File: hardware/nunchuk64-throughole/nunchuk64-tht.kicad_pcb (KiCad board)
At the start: 2 copper layers, 50 x 41.6 mm, 21 parts, among them J1 DB9_Female, J2 DB9_Female, J3 Conn_02x03_Odd_Even, P1 CONN_WII, P2 CONN_WII, Q1 2N7000, Q2 2N7000, Q3 2N7000, Q4 2N7000, SW1 SW_Push, U1 LP2950-3.3_TO92, U2 ATmega328P-PU

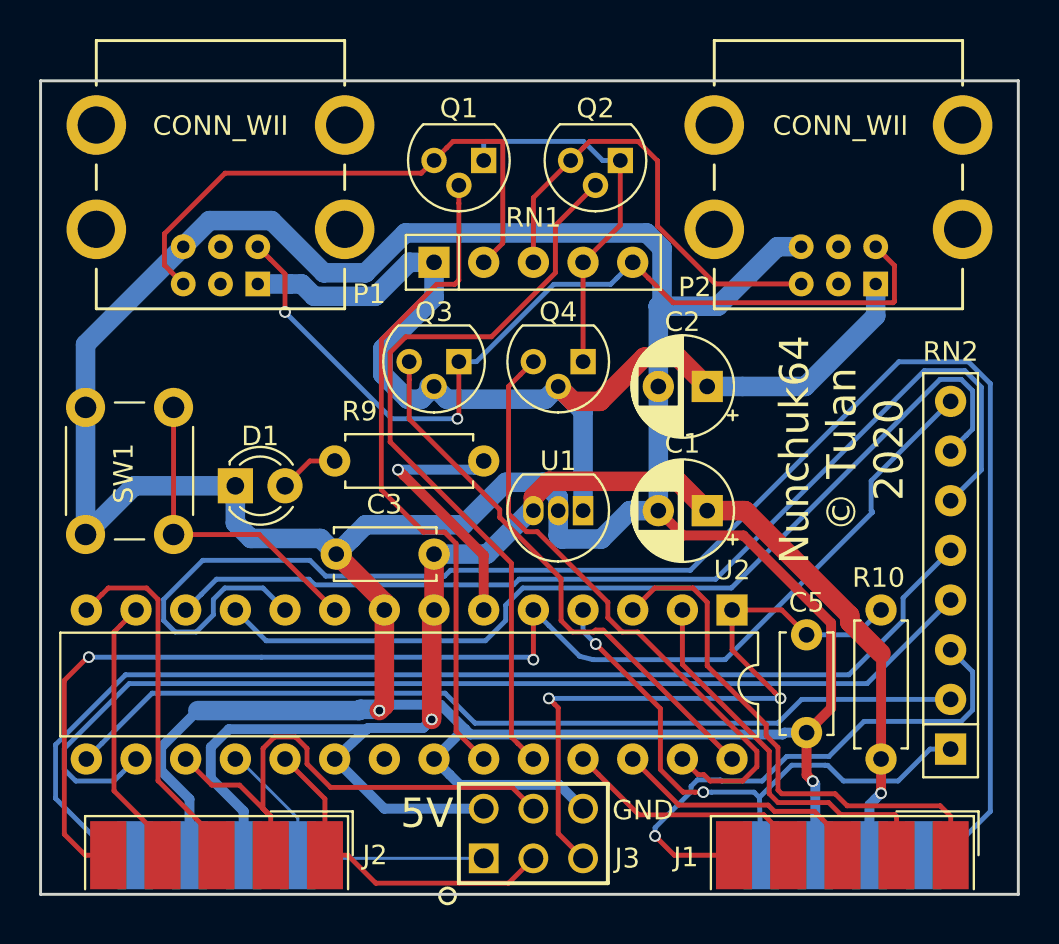
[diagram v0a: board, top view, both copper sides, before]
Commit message: nunchuk64-throughole version. bom with mouser parts.
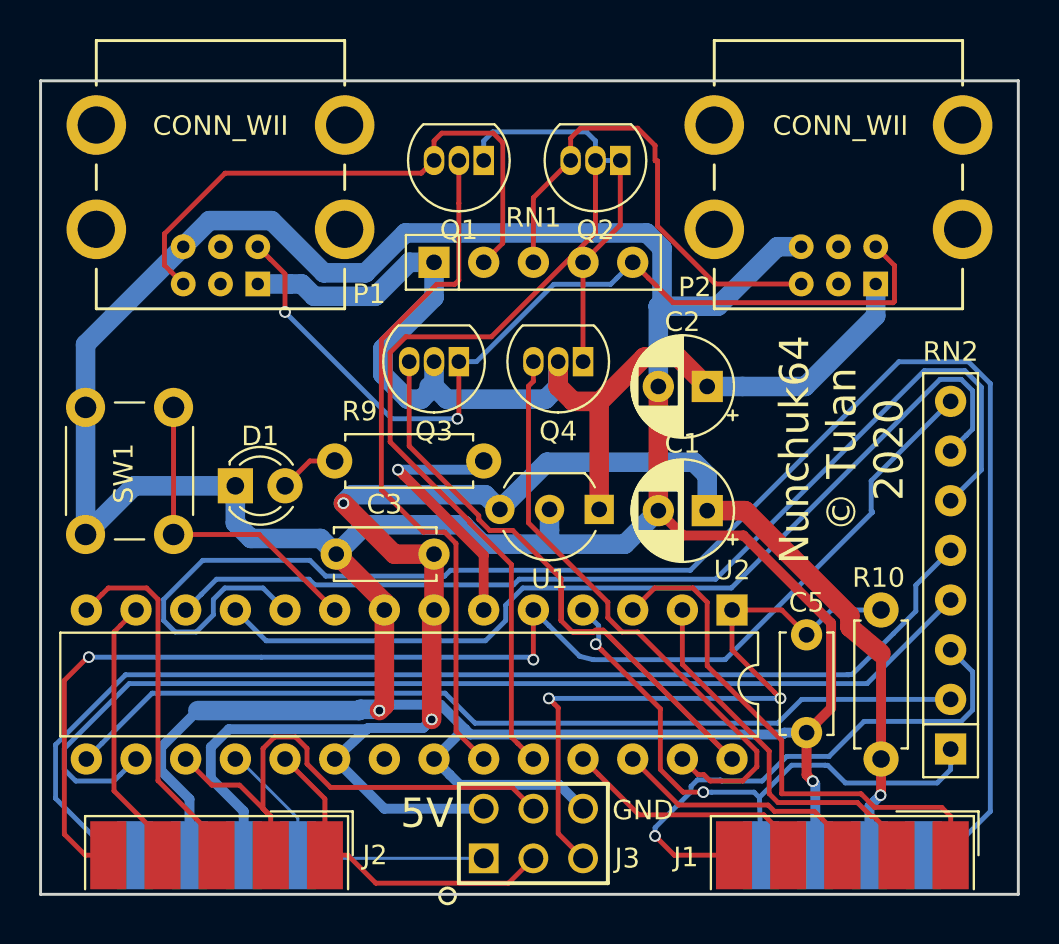
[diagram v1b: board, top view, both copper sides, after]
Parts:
- Q1, Q2, Q3, Q4: footprint Package_TO_SOT_THT:TO-92 -> Package_TO_SOT_THT:TO-92_Inline
- U1: footprint Package_TO_SOT_THT:TO-92_Inline -> Package_TO_SOT_THT:TO-92_Inline_Wide
- moved U1 0.83 mm to (105.0, 93.9)
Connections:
- P1 pad 3: (no net) -> Net-(P1-Pad3)
- P1 pad 4: (no net) -> Net-(P1-Pad4)
- P2 pad 3: (no net) -> Net-(P2-Pad3)
- P2 pad 4: (no net) -> Net-(P2-Pad4)
- Q1 pad 1: /SDA -> /SEL2
- Q2 pad 1: /SDA -> /SEL2
- Q4 pad 1: /SDA -> /SEL2
- RN1 pad 4: /SDA -> /SEL2
- U2 pad 21: (no net) -> Net-(U2-Pad21)
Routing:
- net /SEL2: track 39.3 -> 60.6 mm
- net /SDA: track 19.4 -> 0.00 mm
- net /SCL_: track 28.2 -> 41.5 mm
- net +5V: track 79.5 -> 90.9 mm, vias 2 -> 3
- net +3V3: track 55.5 -> 58.0 mm
- net /SDA2: track 23.2 -> 24.8 mm
- net /SEL1: track 34.3 -> 35.6 mm
- net /SDA_: track 31.9 -> 30.7 mm
- net GND: track 201.2 -> 200.2 mm
- net /SDA1: track 28.8 -> 29.7 mm
- net /Pot_AX: track 29.9 -> 30.7 mm
- net /Joy_A1: track 20.2 -> 19.5 mm

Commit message: fixed problem with traces shortcircuiting
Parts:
- moved Q4 0.06 mm to (104.1, 86.4)
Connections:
- Q1 pad 1: /SEL2 -> /SDA
- Q2 pad 1: /SEL2 -> /SDA
- Q4 pad 1: /SEL2 -> /SDA
- RN1 pad 4: /SEL2 -> /SDA
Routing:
- net /SDA: track 0.00 -> 20.3 mm
- net /SEL2: track 60.6 -> 40.6 mm
